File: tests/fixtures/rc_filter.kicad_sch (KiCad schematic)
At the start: 3 parts

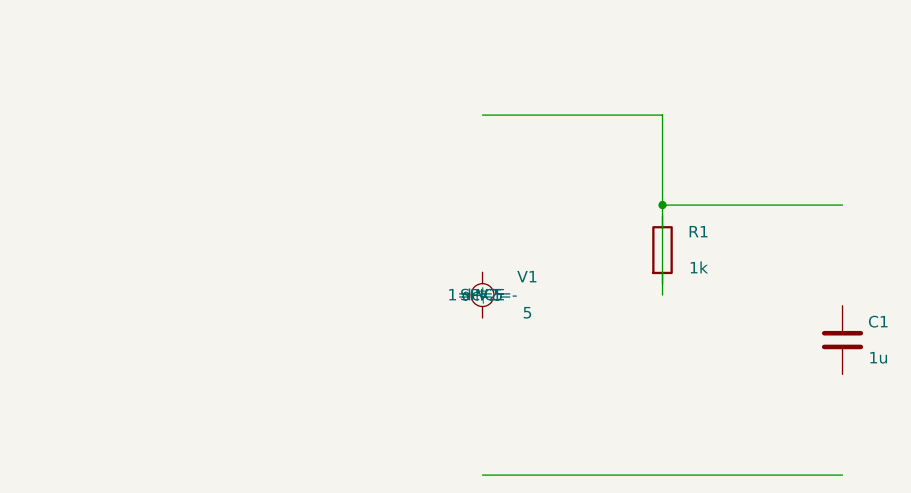
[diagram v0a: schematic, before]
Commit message: T008 phase 5 (scope-reduced): RC fixture rewrite + acceptance + GND→0
Phase 5 закрыта scope-reduced: только RC-фильтр как acceptance.
SE-amp / rectifier фикстуры вынесены в T100 (после интеграции
`kicad-sch-api`, чтобы не делать tube subckt руками в s-expr).
RC-фильтр покрывает все 3 типа анализа (OP / TRAN / AC), pipeline
KiCad → kicad-cli → ngspice → SimulationResult полностью доказан.

Fixture (`tests/fixtures/rc_filter.kicad_sch`):
- Полное переписывание: оригинал T004 имел неподключенные wires
  (все nets как `unconnected-*`), kicad-cli создавал nonsense
  netlist, ngspice падал на «Timestep too small». StubSimulator
  раньше маскировал это, не делая реальной симуляции.
- Layout: V1 (rotation 180, "+" сверху) → R1 (horizontal) →
  C1 (horizontal) → ground (два `power:GND` symbols).
- Sim.* properties (Type/Pins/Device/Library/Params) — `(hide yes)`,
  чтобы не overlay'ились в GUI.
- Power:GND symbol — взят из официальной KiCad library
  (`gitlab.com/kicad/libraries/kicad-symbols`); прежняя моя
  copy-paste версия валила KiCad GUI в overflow (отсутствовал
  `(power global)` flag).

Adapter (`src/adapters/outbound/ngspice/wrapper.py`):
- `_normalize_ground`: token-wise substitution `\bGND\b → 0`. KiCad
  SPICE export использует Value power-symbol'а как net name (`GND`),
  ngspice требует `0`. Изолирует quirk внутри ngspice адаптера.

Acceptance (`tests/e2e/spice_acceptance/test_rc_filter.py`):
- 4 тестов под `@needs_kicad @needs_ngspice`: OP (V≈1V), TRAN
  (steady DC), AC (|H(fc)|≈0.707 на 159Hz, |H|≈1 на 1Hz).
- Прямой вызов `KicadCliSchematicExporter` + `NgspiceSimulator`
  (без CLI); проверяет физику, не CLI message.
- Знак V инвертирован из-за KiCad SPICE pin-order quirk —
  проверки через `abs()`.

Тесты wrapper.py: добавлены 2 теста на `GND → 0` substitution
(positive + edge case с AGND/DGND).

CLI e2e (`tests/e2e/walking_skeleton/test_bridge_design_to_sim.py`):
теперь ожидает `exit 0 + 'Simulation: completed'` (фикстура
работает, ngspice не падает).

BACKL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
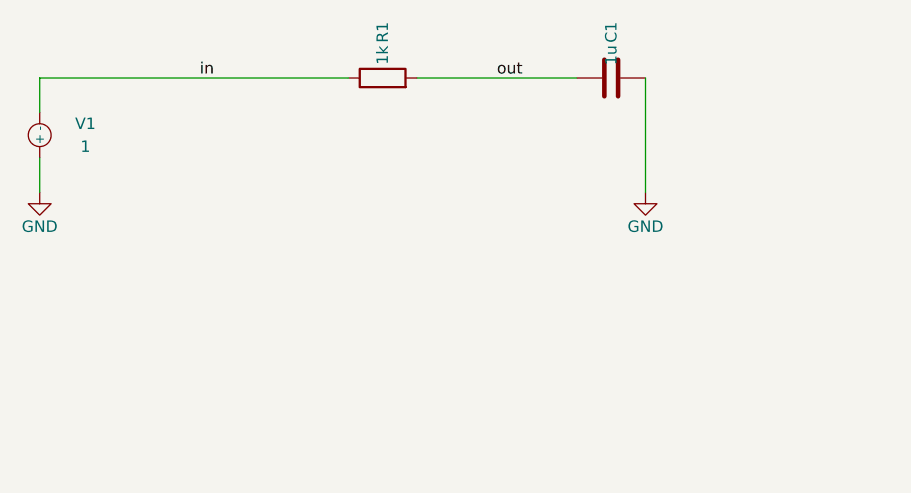
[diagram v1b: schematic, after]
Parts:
- V1: value 5 -> 1
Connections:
- net GND: now reaches V1.1 (+)
- net GND: now also C1.2
- net in: now reaches V1.2 (-)
- net in: now also R1.1
- net out: now reaches R1.2
- net out: now also C1.1
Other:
- moved on the sheet: C1, R1, V1
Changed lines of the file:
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@@
 	(generator_version "10.0")
 	(paper "A4")
-	(junction (at 120 70) (diameter 0) (color 0 0 0 0))
-	(wire (pts (xy 100 60) (xy 120 60)) (stroke (width 0) (type default)))
-	(wire (pts (xy 120 60) (xy 120 70)) (stroke (width 0) (type default)))
-	(wire (pts (xy 120 70) (xy 120 80)) (stroke (width 0) (type default)))
-	(wire (pts (xy 140 70) (xy 120 70)) (stroke (width 0) (type default)))
-	(wire (pts (xy 100 100) (xy 140 100)) (stroke (width 0) (type default)))
-	(symbol (lib_id "Simulation_SPICE:VDC") (at 100 80 0) (unit 1) (exclude_from_sim no) (in_bom yes) (on_board yes) (dnp no)
-		(property "Reference" "V1" (at 105 78 0))
-		(property "Value" "5" (at 105 82 0))
-		(property "Sim.Pins" "1=+ 2=-" (at 100 80 0))
-		(property "Sim.Type" "V" (at 100 80 0))
-		(property "Sim.Device" "SPICE" (at 100 80 0))
-		(property "Sim.Params" "dc=5" (at 100 80 0))
+	(wire (pts (xy 50.8 59.69) (xy 50.8 55.88)) (stroke (width 0) (type default)))
+	(wire (pts (xy 50.8 55.88) (xy 85.09 55.88)) (stroke (width 0) (type default)))
+	(wire (pts (xy 92.71 55.88) (xy 110.49 55.88)) (stroke (width 0) (type default)))
+	(wire (pts (xy 118.11 55.88) (xy 118.11 68.58)) (stroke (width 0) (type default)))
+	(wire (pts (xy 50.8 64.77) (xy 50.8 68.58)) (stroke (width 0) (type default)))
+	(symbol (lib_id "power:GND") (at 50.8 68.58 0) (unit 1) (exclude_from_sim no) (in_bom yes) (on_board yes) (dnp no)
+		(property "Reference" "#PWR01" (at 50.8 74.93 0) (effects (font (size 1.27 1.27)) (hide yes)))
+		(property "Value" "GND" (at 50.8 72.39 0) (effects (font (size 1.27 1.27))))
+		(pin "1")
+		(instances (project "rc_filter" (path "/00000000-0000-0000-0000-000000000001" (reference "#PWR01") (unit 1))))
+	)
+	(symbol (lib_id "power:GND") (at 118.11 68.58 0) (unit 1) (exclude_from_sim no) (in_bom yes) (on_board yes) (dnp no)
+		(property "Reference" "#PWR02" (at 118.11 74.93 0) (effects (font (size 1.27 1.27)) (hide yes)))
+		(property "Value" "GND" (at 118.11 72.39 0) (effects (font (size 1.27 1.27))))
+		(pin "1")
+		(instances (project "rc_filter" (path "/00000000-0000-0000-0000-000000000001" (reference "#PWR02") (unit 1))))
+	)
+	(label "in" (at 68.58 55.88 0)
+		(effects (font (size 1.27 1.27)) (justify left bottom))
+	)
+	(label "out" (at 101.6 55.88 0)
+		(effects (font (size 1.27 1.27)) (justify left bottom))
+	)
+	(symbol (lib_id "Simulation_SPICE:VDC") (at 50.8 62.23 180) (unit 1) (exclude_from_sim no) (in_bom yes) (on_board yes) (dnp no)
+		(property "Reference" "V1" (at 55.88 60.96 0))
+		(property "Value" "1" (at 55.88 63.5 0))
+		(property "Footprint" "" (at 50.8 62.23 0) (effects (font (size 1.27 1.27)) (hide yes)))
+		(property "Datasheet" "" (at 50.8 62.23 0) (effects (font (size 1.27 1.27)) (hide yes)))
+		(property "Sim.Pins" "1=+ 2=-" (at 50.8 62.23 0) (effects (font (size 1.27 1.27)) (hide yes)))
+		(property "Sim.Type" "V" (at 50.8 62.23 0) (effects (font (size 1.27 1.27)) (hide yes)))
+		(property "Sim.Device" "SPICE" (at 50.8 62.23 0) (effects (font (size 1.27 1.27)) (hide yes)))
+		(property "Sim.Library" "" (at 50.8 62.23 0) (effects (font (size 1.27 1.27)) (hide yes)))
+		(property "Sim.Params" "dc=1 ac=1" (at 50.8 62.23 0) (effects (font (size 1.27 1.27)) (hide yes)))
 		(pin "1")
 		(pin "2")
 		(instances (project "rc_filter" (path "/00000000-0000-0000-0000-000000000001" (reference "V1") (unit 1))))
 	)
-	(symbol (lib_id "Device:R") (at 120 75 0) (unit 1) (exclude_from_sim no) (in_bom yes) (on_board yes) (dnp no)
-		(property "Reference" "R1" (at 124 73 0))
-		(property "Value" "1k" (at 124 77 0))
+	(symbol (lib_id "Device:R") (at 88.9 55.88 90) (unit 1) (exclude_from_sim no) (in_bom yes) (on_board yes) (dnp no)
+		(property "Reference" "R1" (at 88.9 50.8 0))
+		(property "Value" "1k" (at 88.9 53.34 0))
+		(property "Footprint" "" (at 88.9 55.88 0) (effects (font (size 1.27 1.27)) (hide yes)))
+		(property "Datasheet" "" (at 88.9 55.88 0) (effects (font (size 1.27 1.27)) (hide yes)))
 		(pin "1")
 		(pin "2")
 		(instances (project "rc_filter" (path "/00000000-0000-0000-0000-000000000001" (reference "R1") (unit 1))))
 	)
-	(symbol (lib_id "Device:C") (at 140 85 0) (unit 1) (exclude_from_sim no) (in_bom yes) (on_board yes) (dnp no)
-		(property "Reference" "C1" (at 144 83 0))
-		(property "Value" "1u" (at 144 87 0))
+	(symbol (lib_id "Device:C") (at 114.3 55.88 90) (unit 1) (exclude_from_sim no) (in_bom yes) (on_board yes) (dnp no)
+		(property "Reference" "C1" (at 114.3 50.8 0))
+		(property "Value" "1u" (at 114.3 53.34 0))
+		(property "Footprint" "" (at 114.3 55.88 0) (effects (font (size 1.27 1.27)) (hide yes)))
+		(property "Datasheet" "" (at 114.3 55.88 0) (effects (font (size 1.27 1.27)) (hide yes)))
 		(pin "1")
 		(pin "2")
